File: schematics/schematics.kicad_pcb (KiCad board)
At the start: 2 copper layers, 50 x 25 mm, 49 parts, among them J1 USB_C_Receptacle_USB2.0_14P, J2 BAT, J3 BT1, J4 BT2, J5 BT3, SW1 SW_SPDT, U1 ESP32-C3-WROOM-02, U2 SPX3819M5-L-3-3, U3 SPX3819M5-L-3-3, U4 LTC4054ES5-4.2, U5 TVS1400DRV

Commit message: completed electronics, ordered parts
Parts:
- removed C1: 1u, Capacitor_SMD:C_0805_2012Metric
- added C15: 1u, Capacitor_SMD:C_0805_2012Metric, F.Cu at (174.2, 95.1)
- SW1: footprint Button_Switch_SMD:SW_SPDT_PCM12 -> Button_Switch_THT:SW_Slide_SPDT_Angled_CK_OS102011MA1Q
- moved C9 42.4 mm to (134.3, 80.7), turned to 180 degrees
- moved C10 40.6 mm to (174.2, 97.5), turned to 0 degrees
- moved U3 5.14 mm to (138.4, 85.0), turned to 90 degrees
- moved C14 5.01 mm to (137.4, 80.8), turned to 90 degrees
- moved SW1 4.80 mm to (133.7, 85.8)
- moved C12 3.33 mm to (139.2, 80.8), turned to 90 degrees
- renumbered R_PROG to R_PROG1, RST to SW4, BOOT to SW5
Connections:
- C9 pad 1: +5V -> +3V3
- J2 pad 1: Net-(J2-Pin_1) -> GND
- J2 pad 2: GND -> Net-(J2-Pin_2)
- SW1 pad 2: Net-(J2-Pin_1) -> Net-(J2-Pin_2)
- U4 pad 3: Net-(J2-Pin_1) -> Net-(J2-Pin_2)
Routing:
- net Net-(J2-Pin_2): track 0.00 -> 13.3 mm
- net Net-(J2-Pin_1): track 6.80 -> 0.00 mm
- net +3V3: track 121.8 -> 125.3 mm
- net GND: vias 3 -> 5

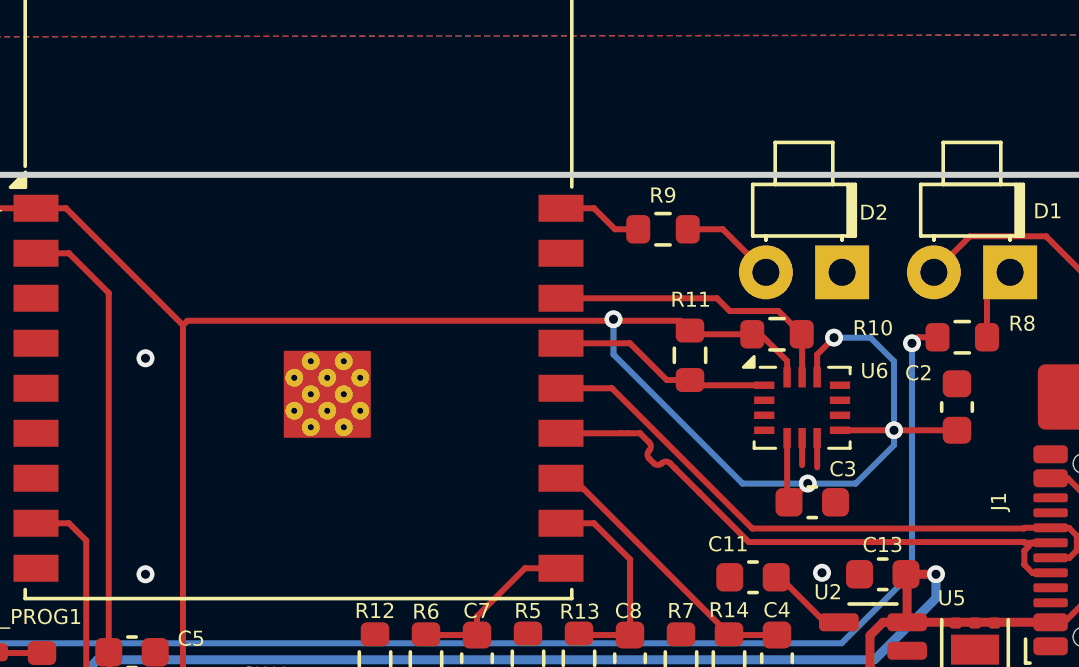
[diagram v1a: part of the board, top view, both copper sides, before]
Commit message: fix i2c pins
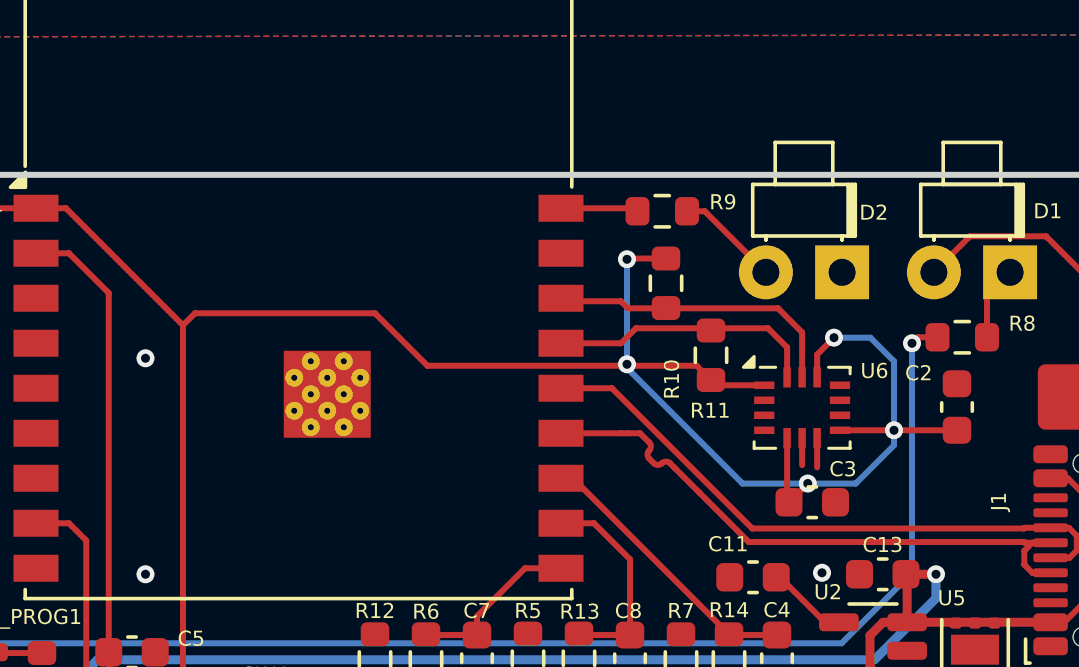
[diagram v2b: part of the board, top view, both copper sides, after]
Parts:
- moved R10 4.07 mm to (162.3, 78.2), turned to -90 degrees
- moved R11 0.70 mm to (163.8, 80.6), turned to 90 degrees
- moved R9 0.60 mm to (162.2, 75.8)
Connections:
- U6 pad 1: /SDA -> +3V3
- U6 pad 14: +3V3 -> /SDA
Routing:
- net +3V3: track 125.3 -> 127.8 mm, vias 6 -> 7
- net /SDA: track 7.35 -> 9.01 mm
